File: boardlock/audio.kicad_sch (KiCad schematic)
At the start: 4 parts

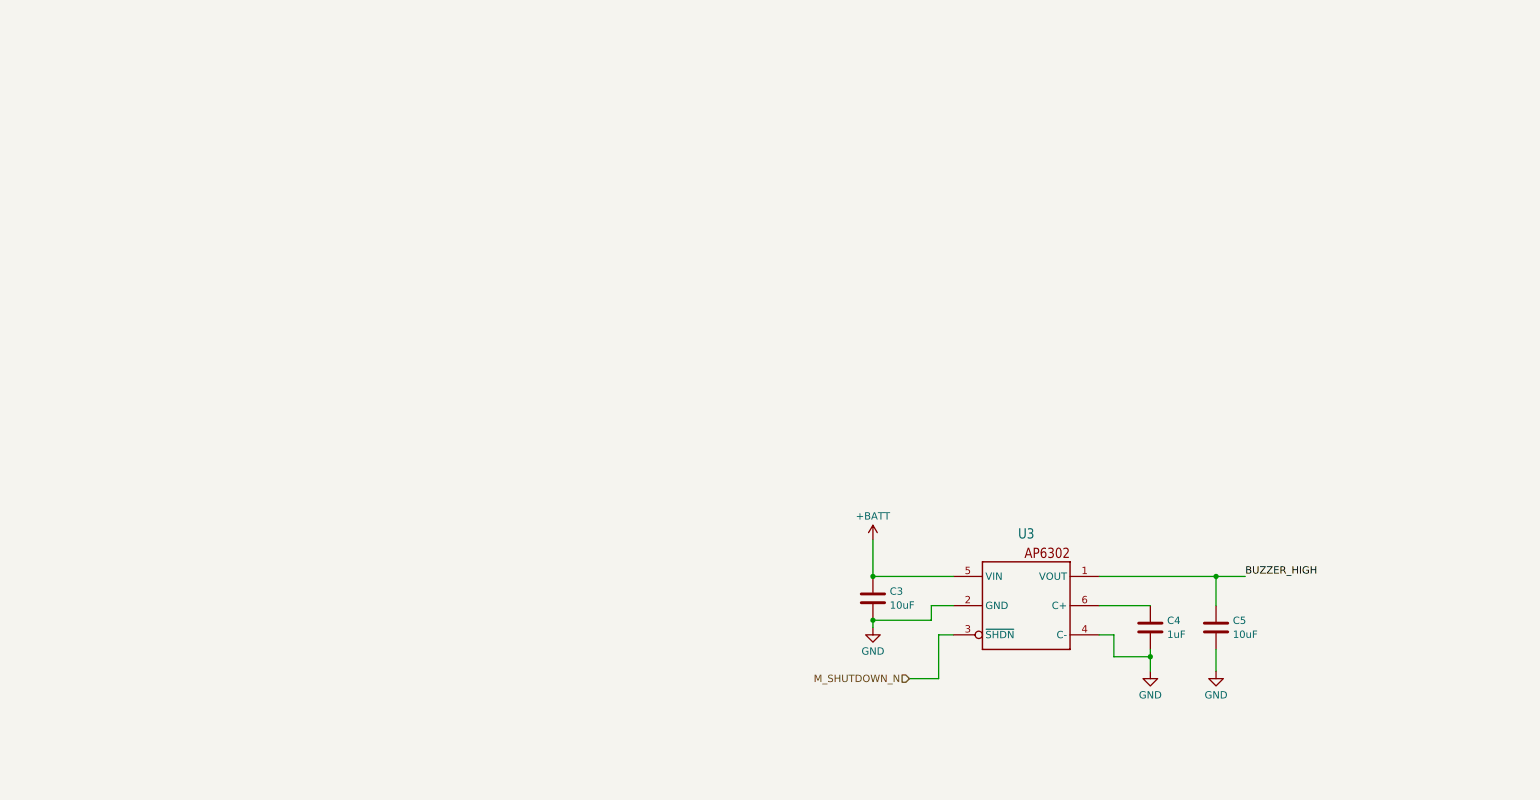
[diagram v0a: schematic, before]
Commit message: Started adding audio schematics
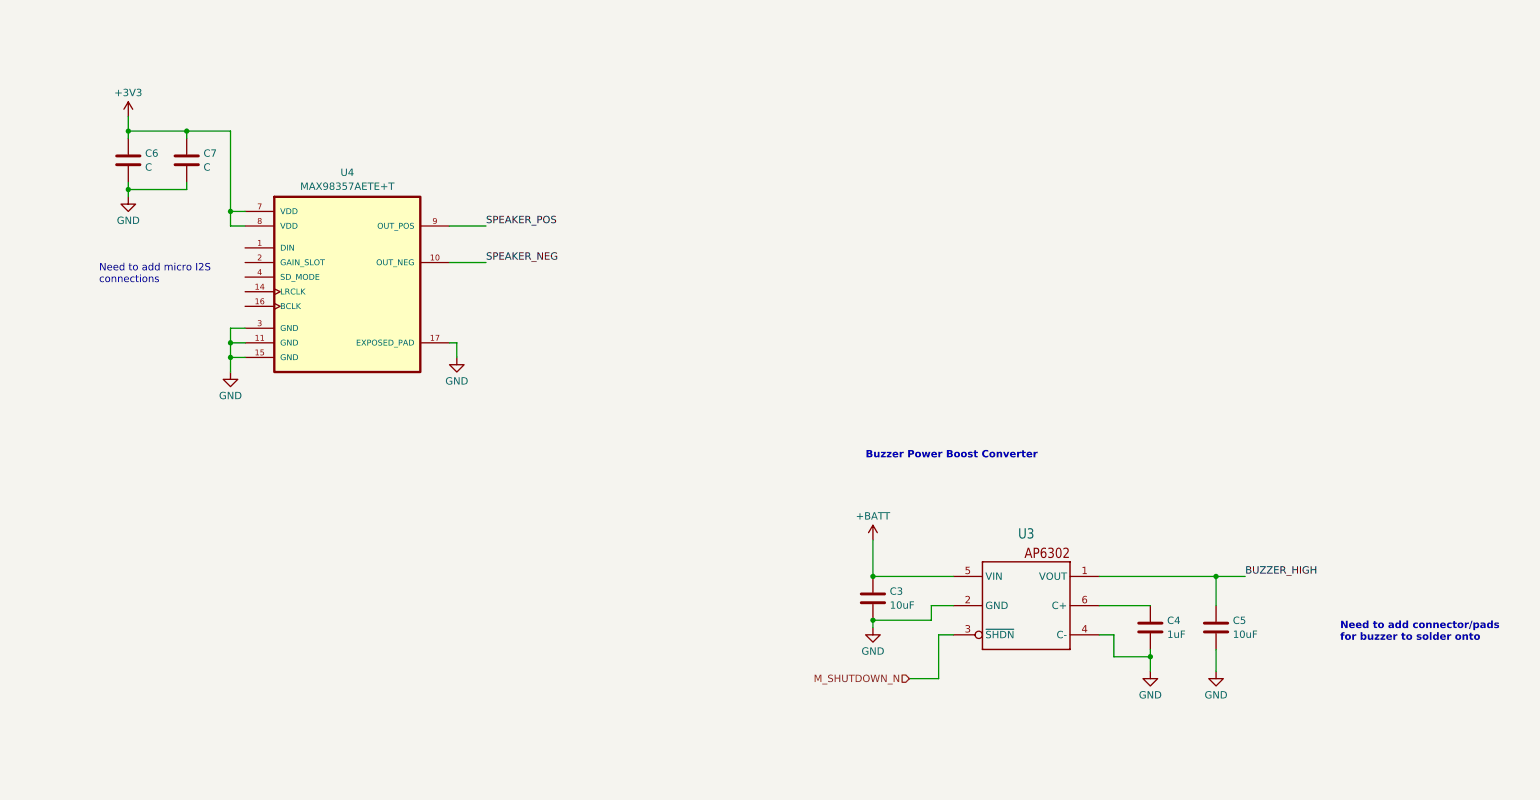
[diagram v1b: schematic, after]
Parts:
- added C6, C7: C, symbol Device:C
- added U4: MAX98357AETE+T, MAX98357AETE+T:QFN50P300X300X80-17N, symbol custom_library:MAX98357AETE+T
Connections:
- net GND: now also C6.2, C7.2, U4.11 (GND), U4.15 (GND), U4.17 (EXPOSED_PAD), U4.3 (GND)
- new net +3V3: C6.1, C7.1, U4.7 (VDD), U4.8 (VDD)
- new net SPEAKER_NEG: U4.10 (OUT_NEG)
- new net SPEAKER_POS: U4.9 (OUT_POS)
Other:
- note added: "Buzzer Power Boost Converter"
- note added: "Need to add connector/pads for buzzer to solder onto"
- note added: "Need to add micro I2S connections"

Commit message: Deleted an error
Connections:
- net +BATT is gone; now on net +3V3: C3.1, U3.5 (VIN)
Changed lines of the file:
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@@
     (effects (font (size 1.27 1.27)) (justify right))
-  )
-  (symbol (lib_id "power:+BATT") (at 171.45 110.49 0) (unit 1)
-    (in_bom yes) (on_board yes) (dnp no) (fields_autoplaced)
-    (property "Reference" "#PWR012" (at 171.45 114.3 0)
-      (effects (font (size 1.27 1.27)) hide)
-    )
-    (property "Value" "+BATT" (at 171.45 106.3569 0)
-      (effects (font (size 1.27 1.27)))
-    )
-    (property "Footprint" "" (at 171.45 110.49 0)
-      (effects (font (size 1.27 1.27)) hide)
-    )
-    (property "Datasheet" "" (at 171.45 110.49 0)
-      (effects (font (size 1.27 1.27)) hide)
-    )
-    (pin "1")
-    (instances
-      (project "boardlock"
-        (path "/e1fc29ce-837e-4062-84d8-c7e423f9eab9/1eb676fb-9e7a-4e01-ba1e-2eff94d7b66e"
-          (reference "#PWR012") (unit 1)
-        )
-      )
-    )
   )
   (symbol (lib_id "Device:C") (at 231.14 125.73 0) (unit 1)
@@
         )
       )
+    )
+  )
+  (symbol (lib_id "power:+3V3") (at 171.45 110.49 0) (unit 1)
+    (in_bom yes) (on_board yes) (dnp no) (fields_autoplaced)
+    (property "Reference" "#PWR012" (at 171.45 114.3 0)
+      (effects (font (size 1.27 1.27)) hide)
+    )
+    (property "Value" "+3V3" (at 171.45 106.3569 0)
+      (effects (font (size 1.27 1.27)))
+    )
+    (property "Footprint" "" (at 171.45 110.49 0)
+      (effects (font (size 1.27 1.27)) hide)
+    )
+    (property "Datasheet" "" (at 171.45 110.49 0)
+      (effects (font (size 1.27 1.27)) hide)
+    )
+    (pin "1")
+    (instances
+      (project "boardlock"
+        (path "/e1fc29ce-837e-4062-84d8-c7e423f9eab9/1eb676fb-9e7a-4e01-ba1e-2eff94d7b66e"
+          (reference "#PWR012") (unit 1)
+        )
+      )

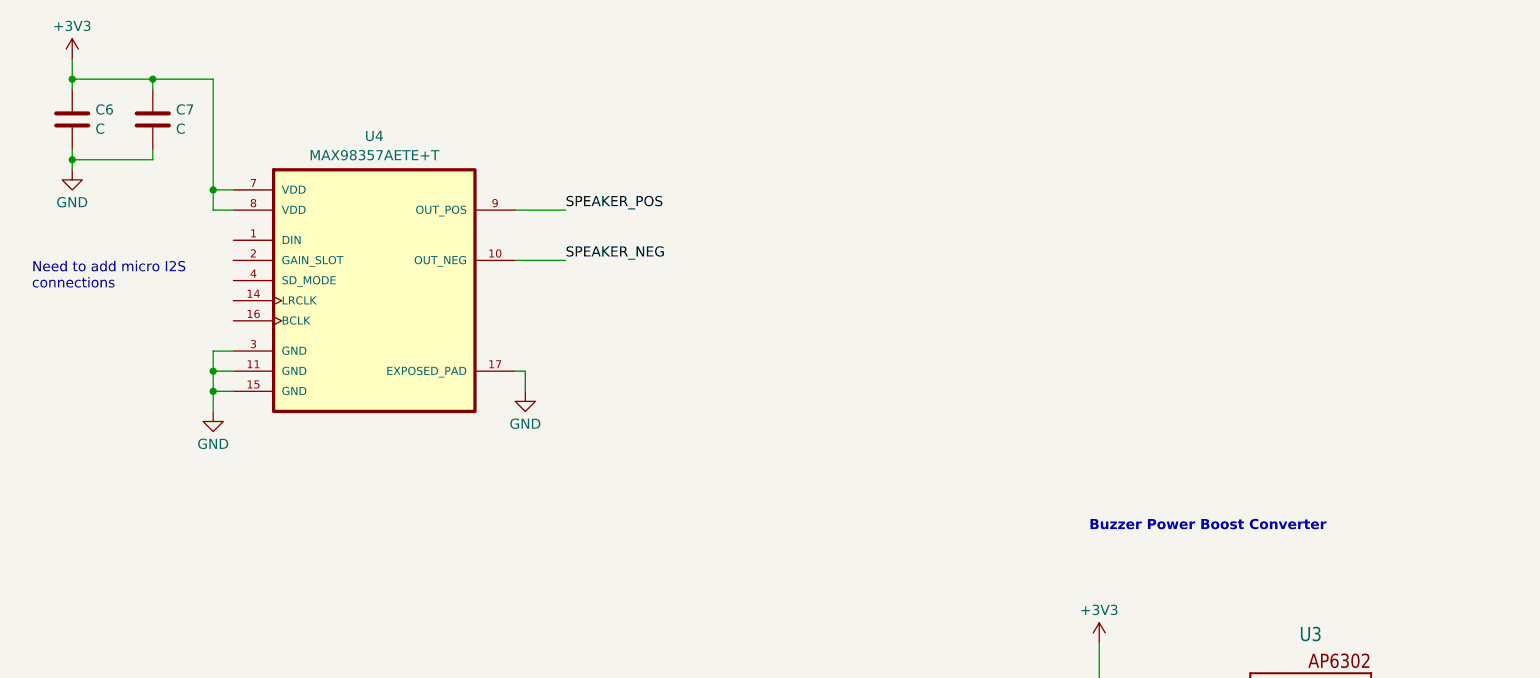
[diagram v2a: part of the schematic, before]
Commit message: Added power library and fixed labels
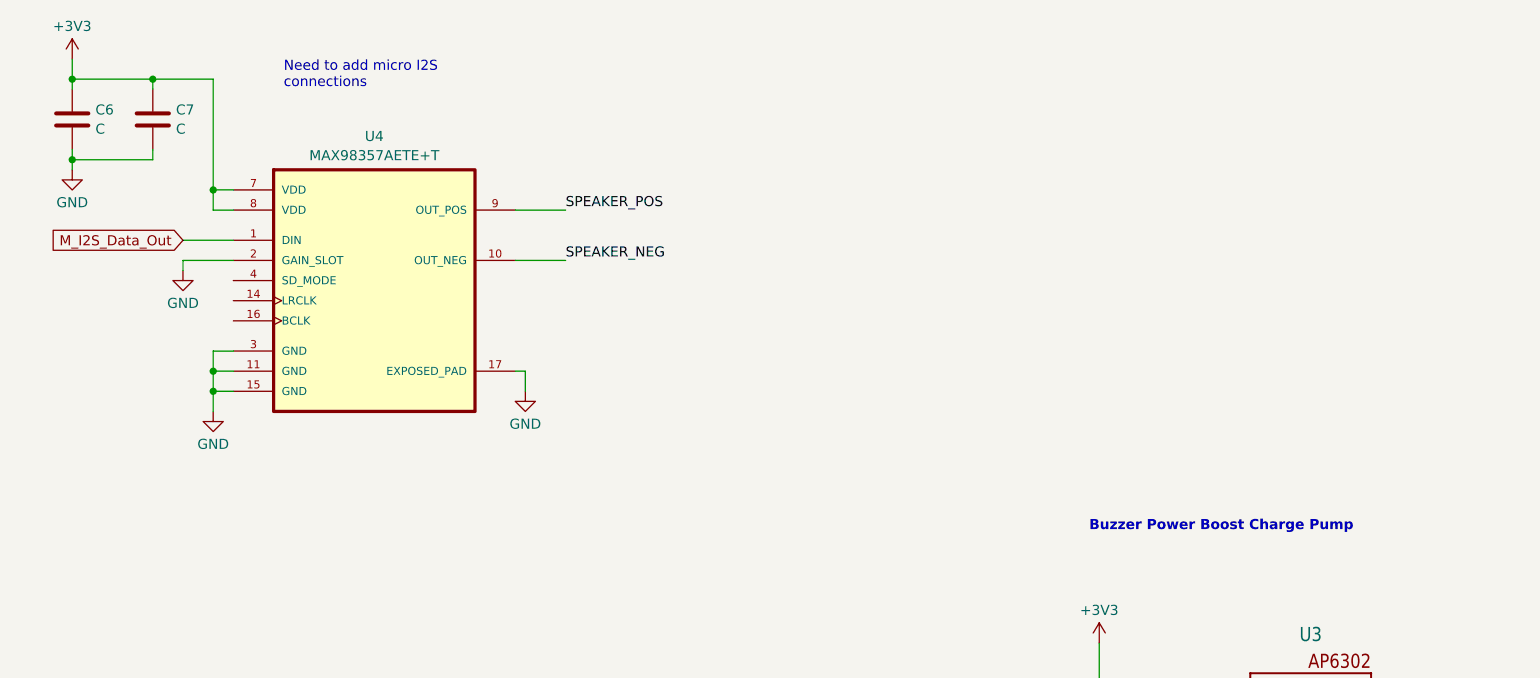
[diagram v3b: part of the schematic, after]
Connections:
- net GND: now also U4.2 (GAIN_SLOT)
- net M_I2S_Data_Out: now reaches U4.1 (DIN)
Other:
- note added: "Buzzer Power Boost Charge Pump"
- note removed: "Buzzer Power Boost Converter"
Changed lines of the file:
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@@
+    (stroke (width 0) (type default))
+  )
+  (wire (pts (xy 62.23 62.23) (xy 55.88 62.23))
+    (stroke (width 0) (type default))
+  )
+  (wire (pts (xy 55.88 62.23) (xy 55.88 63.5))
     (stroke (width 0) (type default))
   )
@@
     (stroke (width 0) (type default))
   )
+  (wire (pts (xy 55.88 59.69) (xy 62.23 59.69))
+    (stroke (width 0) (type default))
+  )
   (wire (pts (xy 181.61 124.46) (xy 181.61 121.92))
     (stroke (width 0) (type default))
   )
-  (text "Buzzer Power Boost Converter" (at 170.18 96.52 0)
+  (text "Buzzer Power Boost Charge Pump" (at 170.18 96.52 0)
     (effects (font (size 1.27 1.27) (thickness 0.254) bold) (justify left bottom))
   )
@@
     (effects (font (size 1.27 1.27) bold) (justify left bottom))
   )
-  (text "Need to add micro I2S\nconnections" (at 36.83 66.04 0)
+  (text "Need to add micro I2S\nconnections" (at 68.58 40.64 0)
     (effects (font (size 1.27 1.27)) (justify left bottom))
   )
@@
   (label "SPEAKER_NEG" (at 104.14 62.23 0) (fields_autoplaced)
     (effects (font (size 1.27 1.27)) (justify left bottom))
+  )
+  (global_label "M_I2S_Data_Out" (shape input) (at 55.88 59.69 180) (fields_autoplaced)
+    (effects (font (size 1.27 1.27)) (justify right))
+    (property "Intersheetrefs" "${INTERSHEET_REFS}" (at 38.0179 59.69 0)
+      (effects (font (size 1.27 1.27)) (justify right) hide)
+    )
   )
   (hierarchical_label "M_SHUTDOWN_N" (shape input) (at 177.8 134.62 180) (fields_autoplaced)
@@
         )
       )
+    )
+  )
+  (symbol (lib_id "power:GND") (at 55.88 63.5 0) (unit 1)
+    (in_bom yes) (on_board yes) (dnp no) (fields_autoplaced)
+    (property "Reference" "#PWR023" (at 55.88 69.85 0)
+      (effects (font (size 1.27 1.27)) hide)
+    )
+    (property "Value" "GND" (at 55.88 67.6331 0)
+      (effects (font (size 1.27 1.27)))
+    )
+    (property "Footprint" "" (at 55.88 63.5 0)
+      (effects (font (size 1.27 1.27)) hide)
+    )
+    (property "Datasheet" "" (at 55.88 63.5 0)
+      (effects (font (size 1.27 1.27)) hide)
+    )
+    (pin "1")
+    (instances
+      (project "boardlock"
+        (path "/e1fc29ce-837e-4062-84d8-c7e423f9eab9/1eb676fb-9e7a-4e01-ba1e-2eff94d7b66e"
+          (reference "#PWR023") (unit 1)
+        )
+      )

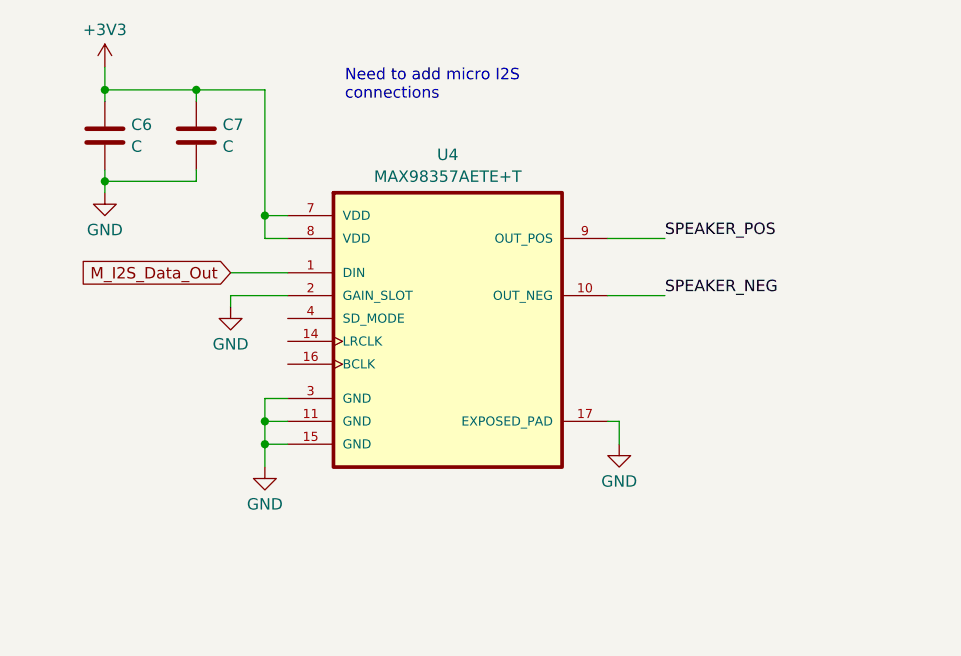
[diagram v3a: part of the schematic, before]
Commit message: updated libraries and edited symbols
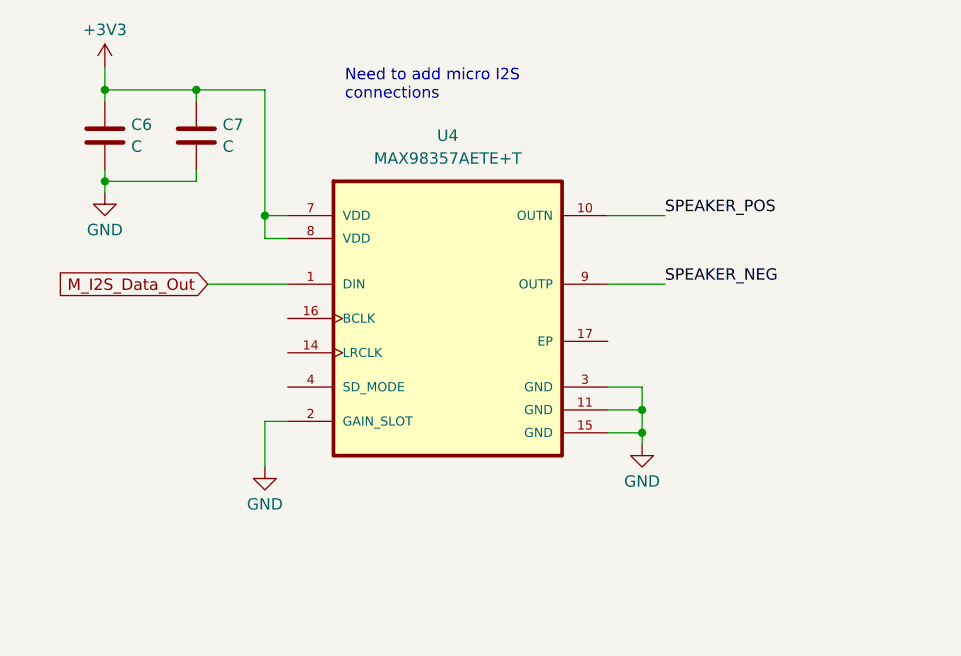
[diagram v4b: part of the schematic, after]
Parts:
- removed U4: MAX98357AETE+T, MAX98357AETE+T:QFN50P300X300X80-17N, symbol custom_library:MAX98357AETE+T
- added U4: MAX98357AETE+T, MAX98357AETE+T:QFN50P300X300X80-17N, symbol MAX98357AETE+T:MAX98357AETE+T
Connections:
- net +3V3: now also U4.7 (VDD), U4.8 (VDD)
- net GND: now also U4.11 (GND), U4.15 (GND), U4.2 (GAIN_SLOT), U4.3 (GND)
- net M_I2S_Data_Out: now also U4.1 (DIN)
- net SPEAKER_NEG: now also U4.9 (OUTP)
- net SPEAKER_POS: now also U4.10 (OUTN)
